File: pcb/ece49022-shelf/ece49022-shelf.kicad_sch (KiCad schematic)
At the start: 0 parts

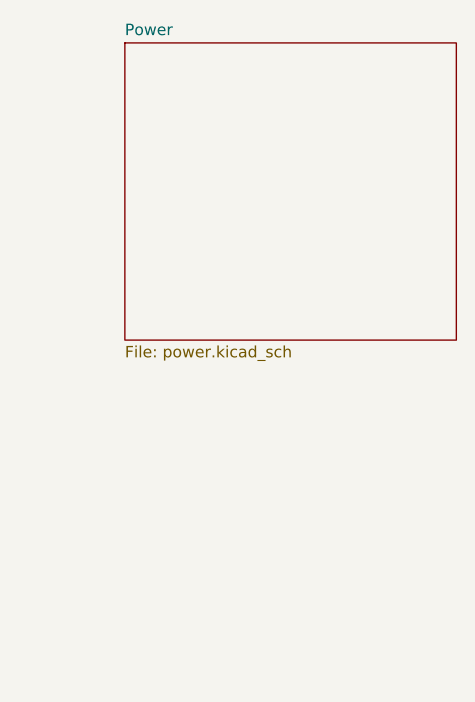
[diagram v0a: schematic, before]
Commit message: Initial Power Schematics Finished
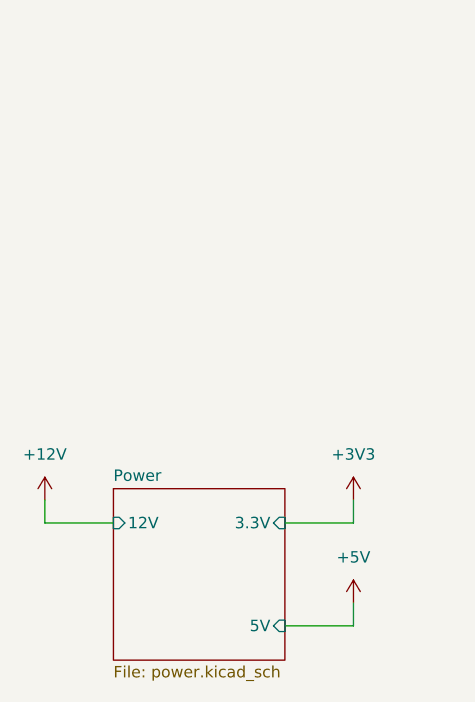
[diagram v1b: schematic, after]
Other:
- sheet Power ports: added 12V, 3.3V, 5V; removed none

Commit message: paths fixed?
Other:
- added sheet RP2350A (rp2350A.kicad_sch)
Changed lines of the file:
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@@
+		)
+	)
+	(sheet
+		(at 95.25 74.93)
+		(size 40.64 63.5)
+		(exclude_from_sim no)
+		(in_bom yes)
+		(on_board yes)
+		(dnp no)
+		(fields_autoplaced yes)
+		(stroke
+			(width 0.1524)
+			(type solid)
+		)
+		(fill
+			(color 0 0 0 0.0000)
+		)
+		(property "Sheetname" "RP2350A"
+			(at 95.25 74.2184 0)
+			(effects
+				(font
+					(size 1.27 1.27)
+				)
+				(justify left bottom)
+			)
+		)
+		(property "Sheetfile" "rp2350A.kicad_sch"
+			(at 95.25 139.0146 0)
+			(effects
+				(font
+					(size 1.27 1.27)
+				)
+				(justify left top)
+			)
+		)
+		(instances
+			(project "ece49022-shelf"
+				(path "/cb6cb1b4-c151-4aa2-8cd7-5430288cfa02"
+					(page "3")
+				)
+			)
 		)
 	)

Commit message: updated schematic
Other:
- added sheet NAU7802 (NAU7802.kicad_sch)
- sheet Power ports: added GND; removed none
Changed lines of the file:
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@@
+	(wire
+		(pts
+			(xy 25.4 97.79) (xy 25.4 102.87)
+		)
+		(stroke
+			(width 0)
+			(type default)
+		)
+	)
 	(wire
 		(pts
@@
 		(pts
 			(xy 25.4 83.82) (xy 25.4 86.36)
+		)
+		(stroke
+			(width 0)
+			(type default)
+		)
+	)
+	(wire
+		(pts
+			(xy 33.02 97.79) (xy 25.4 97.79)
 		)
 		(stroke
@@
 	)
 	(symbol
+		(lib_id "power:GND")
+		(at 25.4 102.87 0)
+		(unit 1)
+		(exclude_from_sim no)
+		(in_bom yes)
+		(on_board yes)
+		(dnp no)
+		(fields_autoplaced yes)
+		(property "Reference" "#PWR015"
+			(at 25.4 109.22 0)
+			(effects
+				(font
+					(size 1.27 1.27)
+				)
+				(hide yes)
+			)
+		)
+		(property "Value" "GND"
+			(at 25.4 107.95 0)
+			(effects
+				(font
+					(size 1.27 1.27)
+				)
+			)
+		)
+		(property "Footprint" ""
+			(at 25.4 102.87 0)
+			(effects
+				(font
+					(size 1.27 1.27)
+				)
+				(hide yes)
+			)
+		)
+		(property "Datasheet" ""
+			(at 25.4 102.87 0)
+			(effects
+				(font
+					(size 1.27 1.27)
+				)
+				(hide yes)
+			)
+		)
+		(property "Description" "Power symbol creates a global label with name \"GND\" , ground"
+			(at 25.4 102.87 0)
+			(effects
+				(font
+					(size 1.27 1.27)
+				)
+				(hide yes)
+			)
+		)
+		(pin "1"
+		)
+		(instances
+			(project ""
+				(path "/cb6cb1b4-c151-4aa2-8cd7-5430288cfa02"
+					(reference "#PWR015")
+					(unit 1)
+				)
+			)
+		)
+	)
+	(symbol
 		(lib_id "power:+5V")
 		(at 59.69 95.25 0)
@@
 			)
 		)
+		(pin "GND" input
+			(at 33.02 97.79 180)
+			(effects
+				(font
+					(size 1.27 1.27)
+				)
+				(justify left)
+			)
+		)
 		(instances
 			(project "ece49022-shelf"
@@
 				)
 			)
+		)
+	)
+	(sheet
+		(at 182.88 72.39)
+		(size 29.21 40.64)
+		(exclude_from_sim no)
+		(in_bom yes)
+		(on_board yes)
+		(dnp no)
+		(fields_autoplaced yes)
+		(stroke
+			(width 0.1524)
+			(type solid)
+		)
+		(fill
+			(color 0 0 0 0.0000)
+		)
+		(property "Sheetname" "NAU7802"
+			(at 182.88 71.6784 0)
+			(effects
+				(font
+					(size 1.27 1.27)
+				)
+				(justify left bottom)
+			)
+		)
+		(property "Sheetfile" "NAU7802.kicad_sch"
+			(at 182.88 113.6146 0)
+			(effects
+				(font
+					(size 1.27 1.27)
+				)
+				(justify left top)
+			)
+		)
+		(instances
+			(project "ece49022-shelf"
+				(path "/cb6cb1b4-c151-4aa2-8cd7-5430288cfa02"
+					(page "4")
+				)
+			)

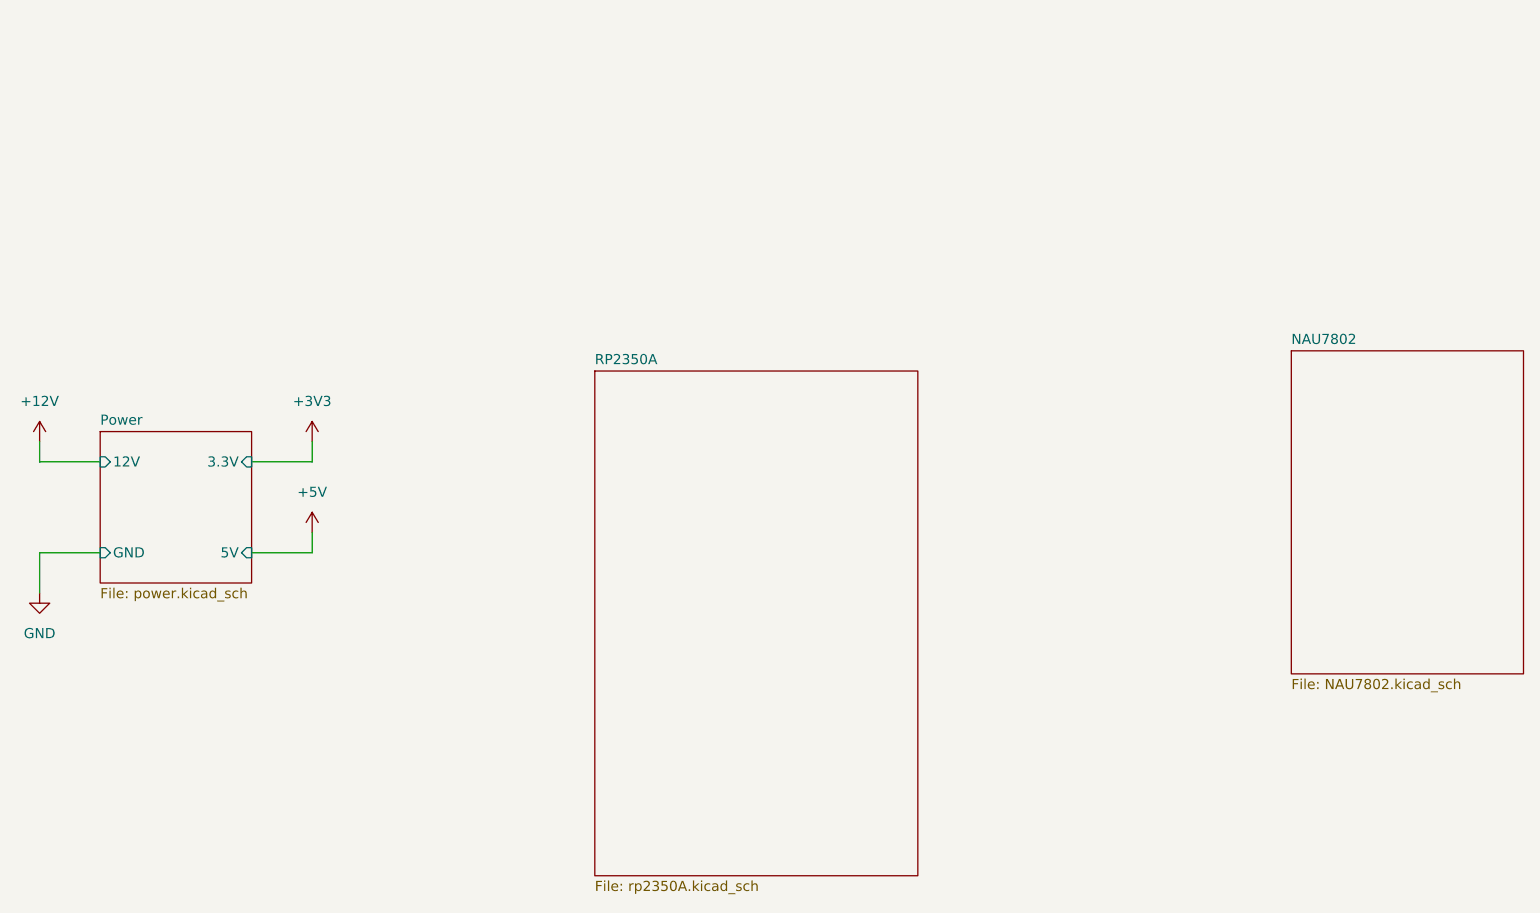
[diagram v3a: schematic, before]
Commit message: rp2350 inside
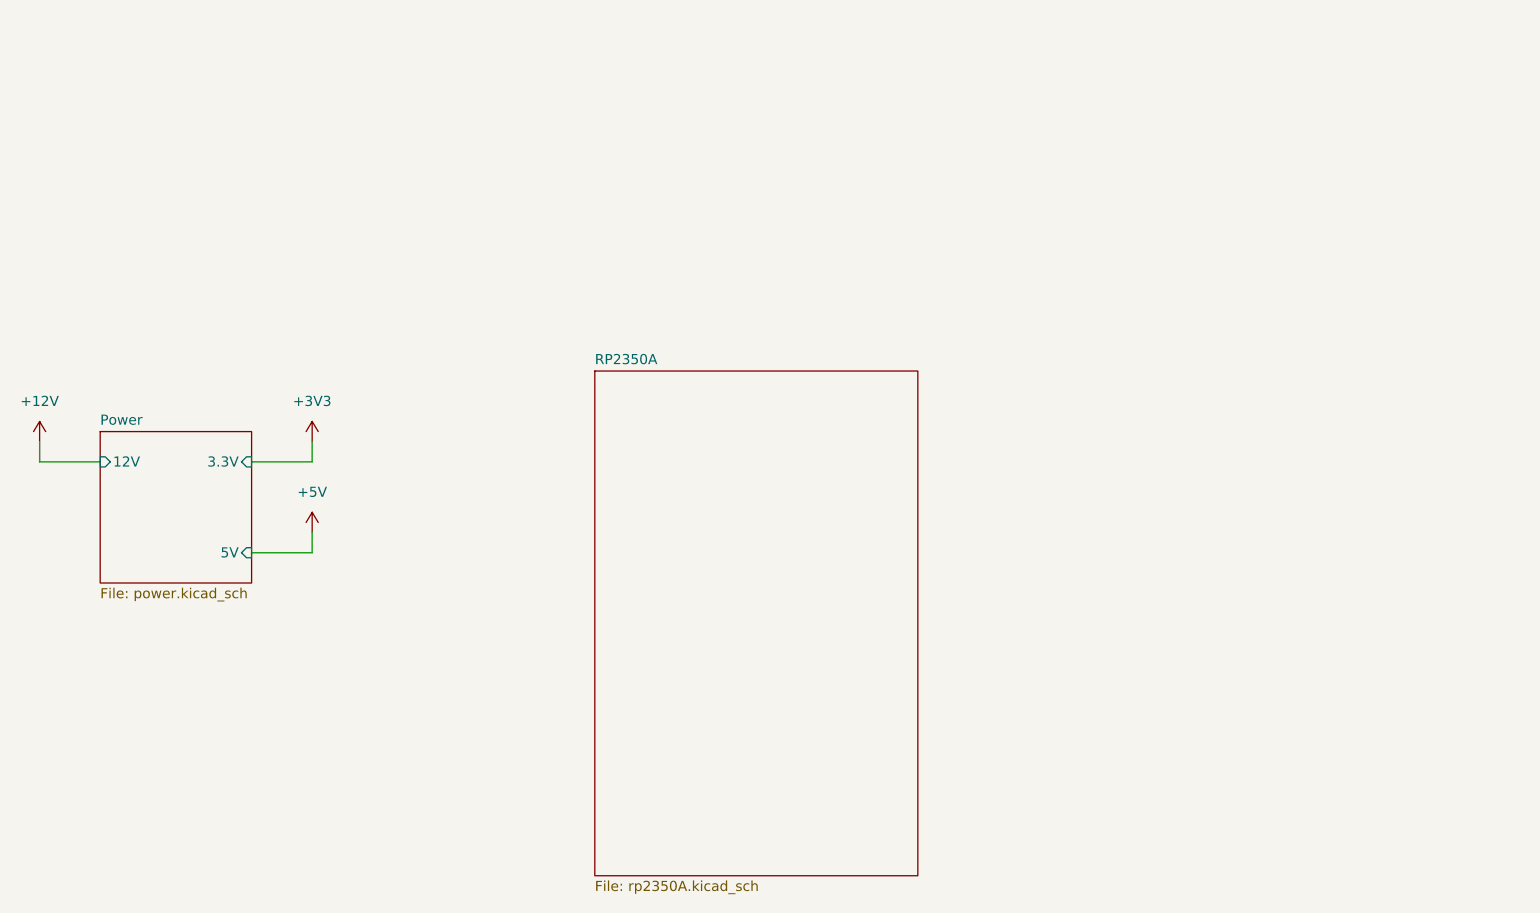
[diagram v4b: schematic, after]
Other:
- removed sheet NAU7802
- sheet Power ports: added none; removed GND
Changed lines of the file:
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@@
-	(wire
-		(pts
-			(xy 25.4 97.79) (xy 25.4 102.87)
-		)
-		(stroke
-			(width 0)
-			(type default)
-		)
-	)
 	(wire
 		(pts
@@
 		(pts
 			(xy 25.4 83.82) (xy 25.4 86.36)
-		)
-		(stroke
-			(width 0)
-			(type default)
-		)
-	)
-	(wire
-		(pts
-			(xy 33.02 97.79) (xy 25.4 97.79)
 		)
 		(stroke
@@
 	)
 	(symbol
-		(lib_id "power:GND")
-		(at 25.4 102.87 0)
-		(unit 1)
-		(exclude_from_sim no)
-		(in_bom yes)
-		(on_board yes)
-		(dnp no)
-		(fields_autoplaced yes)
-		(property "Reference" "#PWR015"
-			(at 25.4 109.22 0)
-			(effects
-				(font
-					(size 1.27 1.27)
-				)
-				(hide yes)
-			)
-		)
-		(property "Value" "GND"
-			(at 25.4 107.95 0)
-			(effects
-				(font
-					(size 1.27 1.27)
-				)
-			)
-		)
-		(property "Footprint" ""
-			(at 25.4 102.87 0)
-			(effects
-				(font
-					(size 1.27 1.27)
-				)
-				(hide yes)
-			)
-		)
-		(property "Datasheet" ""
-			(at 25.4 102.87 0)
-			(effects
-				(font
-					(size 1.27 1.27)
-				)
-				(hide yes)
-			)
-		)
-		(property "Description" "Power symbol creates a global label with name \"GND\" , ground"
-			(at 25.4 102.87 0)
-			(effects
-				(font
-					(size 1.27 1.27)
-				)
-				(hide yes)
-			)
-		)
-		(pin "1"
-		)
-		(instances
-			(project ""
-				(path "/cb6cb1b4-c151-4aa2-8cd7-5430288cfa02"
-					(reference "#PWR015")
-					(unit 1)
-				)
-			)
-		)
-	)
-	(symbol
 		(lib_id "power:+5V")
 		(at 59.69 95.25 0)
@@
 			)
 		)
-		(pin "GND" input
-			(at 33.02 97.79 180)
-			(effects
-				(font
-					(size 1.27 1.27)
-				)
-				(justify left)
-			)
-		)
 		(instances
 			(project "ece49022-shelf"
@@
 				)
 			)
-		)
-	)
-	(sheet
-		(at 182.88 72.39)
-		(size 29.21 40.64)
-		(exclude_from_sim no)
-		(in_bom yes)
-		(on_board yes)
-		(dnp no)
-		(fields_autoplaced yes)
-		(stroke
-			(width 0.1524)
-			(type solid)
-		)
-		(fill
-			(color 0 0 0 0.0000)
-		)
-		(property "Sheetname" "NAU7802"
-			(at 182.88 71.6784 0)
-			(effects
-				(font
-					(size 1.27 1.27)
-				)
-				(justify left bottom)
-			)
-		)
-		(property "Sheetfile" "NAU7802.kicad_sch"
-			(at 182.88 113.6146 0)
-			(effects
-				(font
-					(size 1.27 1.27)
-				)
-				(justify left top)
-			)
-		)
-		(instances
-			(project "ece49022-shelf"
-				(path "/cb6cb1b4-c151-4aa2-8cd7-5430288cfa02"
-					(page "4")
-				)
-			)
